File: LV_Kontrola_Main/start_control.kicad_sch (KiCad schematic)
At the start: 20 parts, among them U4 STM32F103C8Tx, Y1 32.768kHz, Y2 8MHz

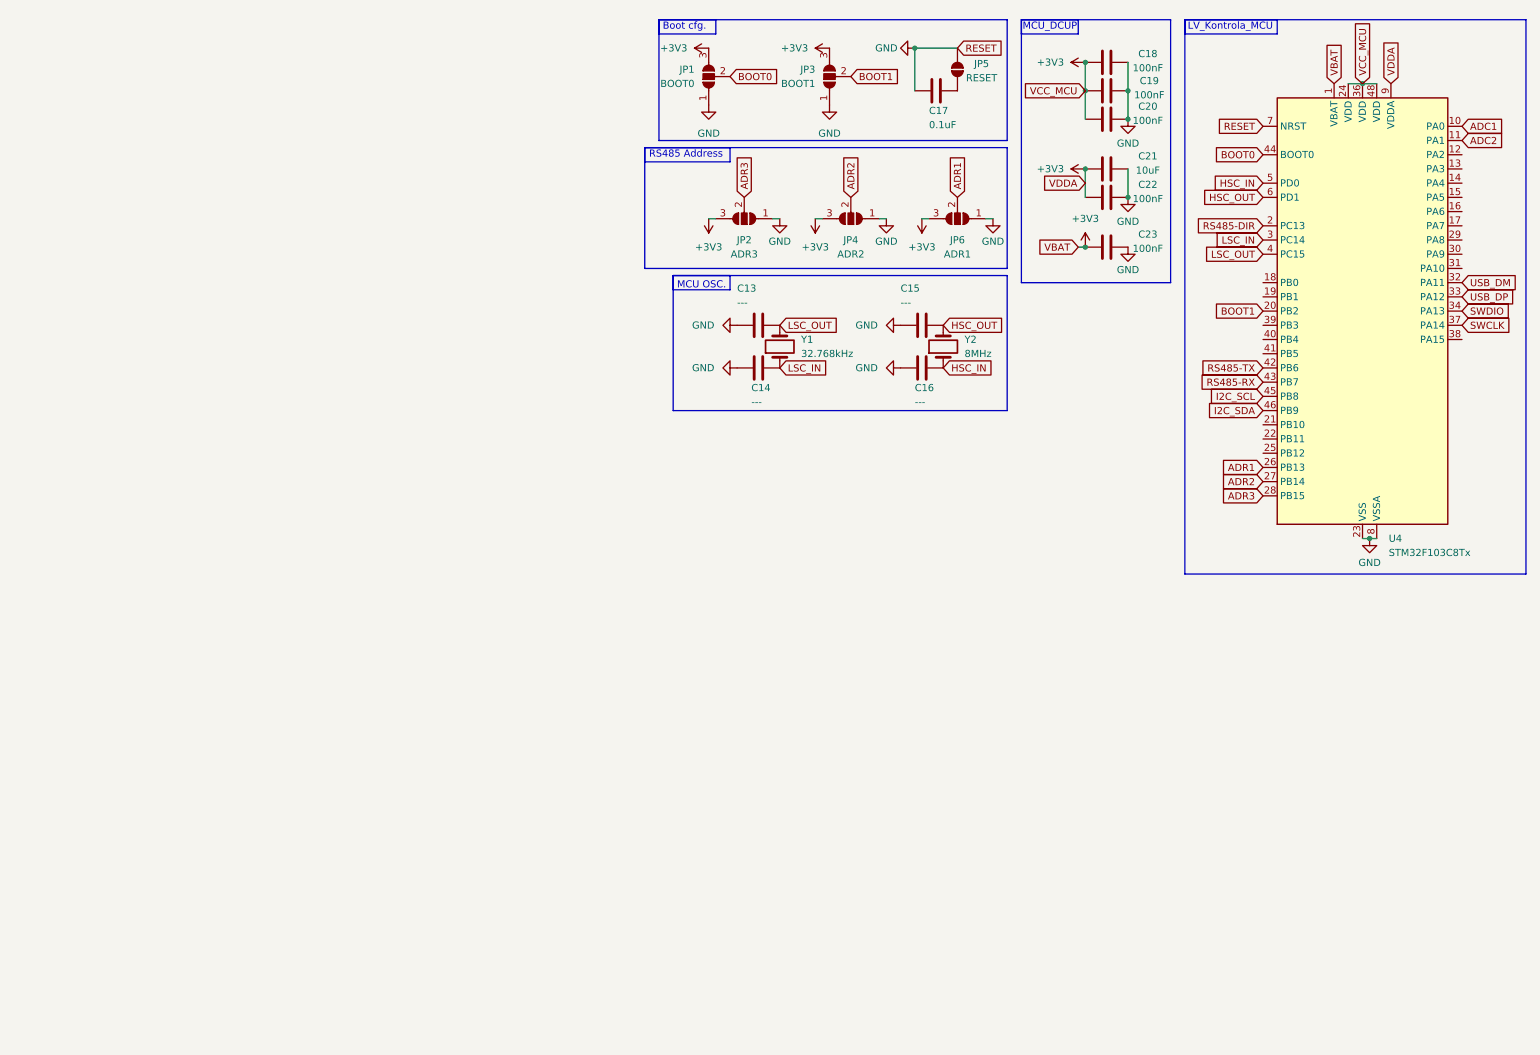
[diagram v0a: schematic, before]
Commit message: Added Start Control
Added Start Control MCU to the LV_Kontrola_Main, added hsc/lsc to LV_Regulator, fixed component numbering
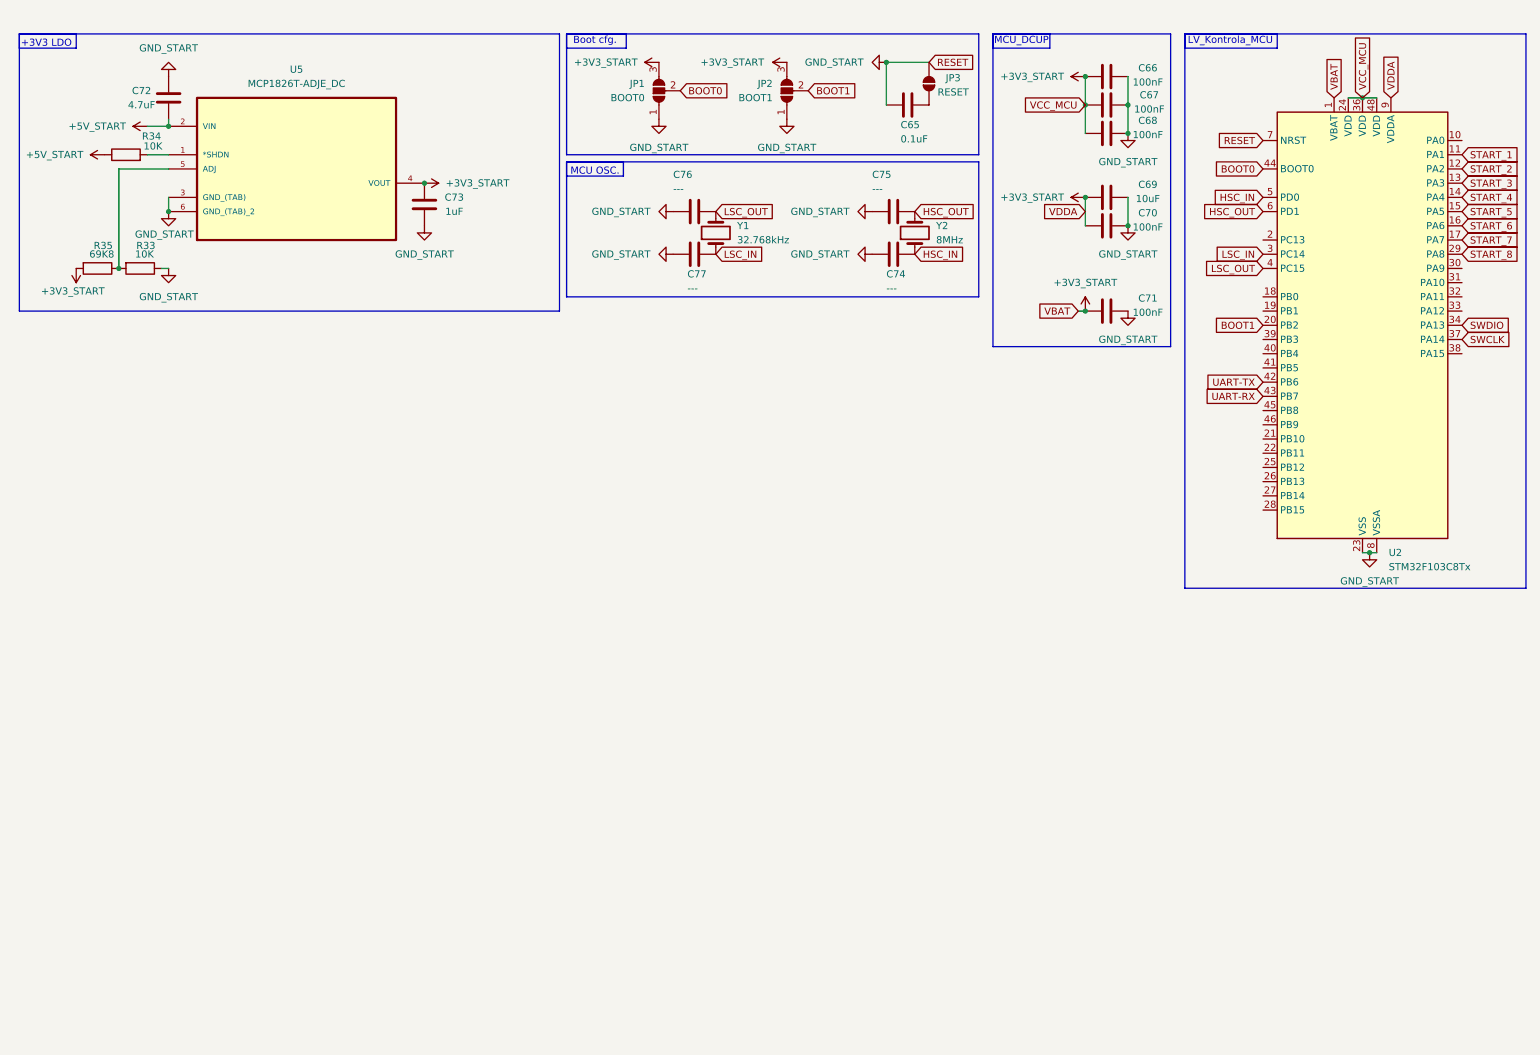
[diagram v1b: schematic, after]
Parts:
- removed C17: 0.1uF, symbol Device:C
- removed C18, C19, C20, C22, C23: 100nF, symbol Device:C
- removed C21: 10uF, symbol Device:C
- removed JP2: ADR3, symbol Jumper:SolderJumper_3_Open
- removed JP4: ADR2, symbol Jumper:SolderJumper_3_Open
- removed JP6: ADR1, symbol Jumper:SolderJumper_3_Open
- added C65: 0.1uF, symbol Device:C
- added C66, C67, C68, C70, C71: 100nF, symbol Device:C
- added C69: 10uF, symbol Device:C
- added C72: 4.7uF, symbol Device:C
- added C73: 1uF, symbol Device:C
- added R33, R34: 10K, symbol Device:R
- added R35: 69K8, symbol Device:R
- added U5: MCP1826T-ADJE_DC, MCP1826T-ADJE_DC:SOT230P700X180-6N, symbol MCP1826T-ADJE_DC:MCP1826T-ADJE_DC
- renumbered C16 to C74, C15 to C75, C13 to C76, C14 to C77, JP3 to JP2, JP5 to JP3, U4 to U2
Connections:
- net at JP3.2 (B): now also C65.1
- net START_2: now reaches U2.12 (PA2)
- net START_3: now reaches U2.13 (PA3)
- net START_4: now reaches U2.14 (PA4)
- net START_5: now reaches U2.15 (PA5)
- net START_6: now reaches U2.16 (PA6)
- net START_7: now reaches U2.17 (PA7)
- net START_8: now reaches U2.29 (PA8)
- net +3V3 renamed +3V3_START
- net +3V3_START: now also C66.1, C67.1, C68.1, C69.1, C70.1, C71.1, C73.2, R33.2, U5.4 (VOUT)
- net ADC1: no longer names the net of U2.10 (PA0)
- net ADC2 renamed START_1
- net ADR1: no longer names the net of U2.26 (PB13)
- net ADR2: no longer names the net of U2.27 (PB14)
- net ADR3: no longer names the net of U2.28 (PB15)
- net GND renamed GND_START
- net GND_START: now also C65.2, C66.2, C67.2, C68.2, C69.2, C70.2, C71.2, C72.1, C73.1, R35.1, U5.3 (GND_(TAB)), U5.6 (GND_(TAB)_2)
- net I2C_SCL: no longer names the net of U2.45 (PB8)
- net I2C_SDA: no longer names the net of U2.46 (PB9)
- net RS485-DIR: no longer names the net of U2.2 (PC13)
- net RS485-RX renamed UART-RX
- net RS485-TX renamed UART-TX
- net USB_DM: no longer names the net of U2.32 (PA11)
- net USB_DP: no longer names the net of U2.33 (PA12)
- new net: R34.2, U5.1 (*SHDN)
- new net: R33.1, R35.2, U5.5 (ADJ)
- new net +5V_START: C72.2, R34.1, U5.2 (VIN)
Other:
- note added: "+3V3 LDO"
- note removed: "RS485 Address"
- company: "Black Horntets" Formula Student team -> "Black Hornets" Formula Student team
- title: LV_Regulator_Main -> LV_Kontrola_Main
- moved on the sheet: C74, C75, C76, C77, JP1, JP2, JP3, U2, Y1, Y2

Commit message: Added Stat logic
Added start mcu and associated components to the LV_Kontrola_Main schematic, added STM32CubeIDE project and basic configuration, added fuses to LV_Regulator
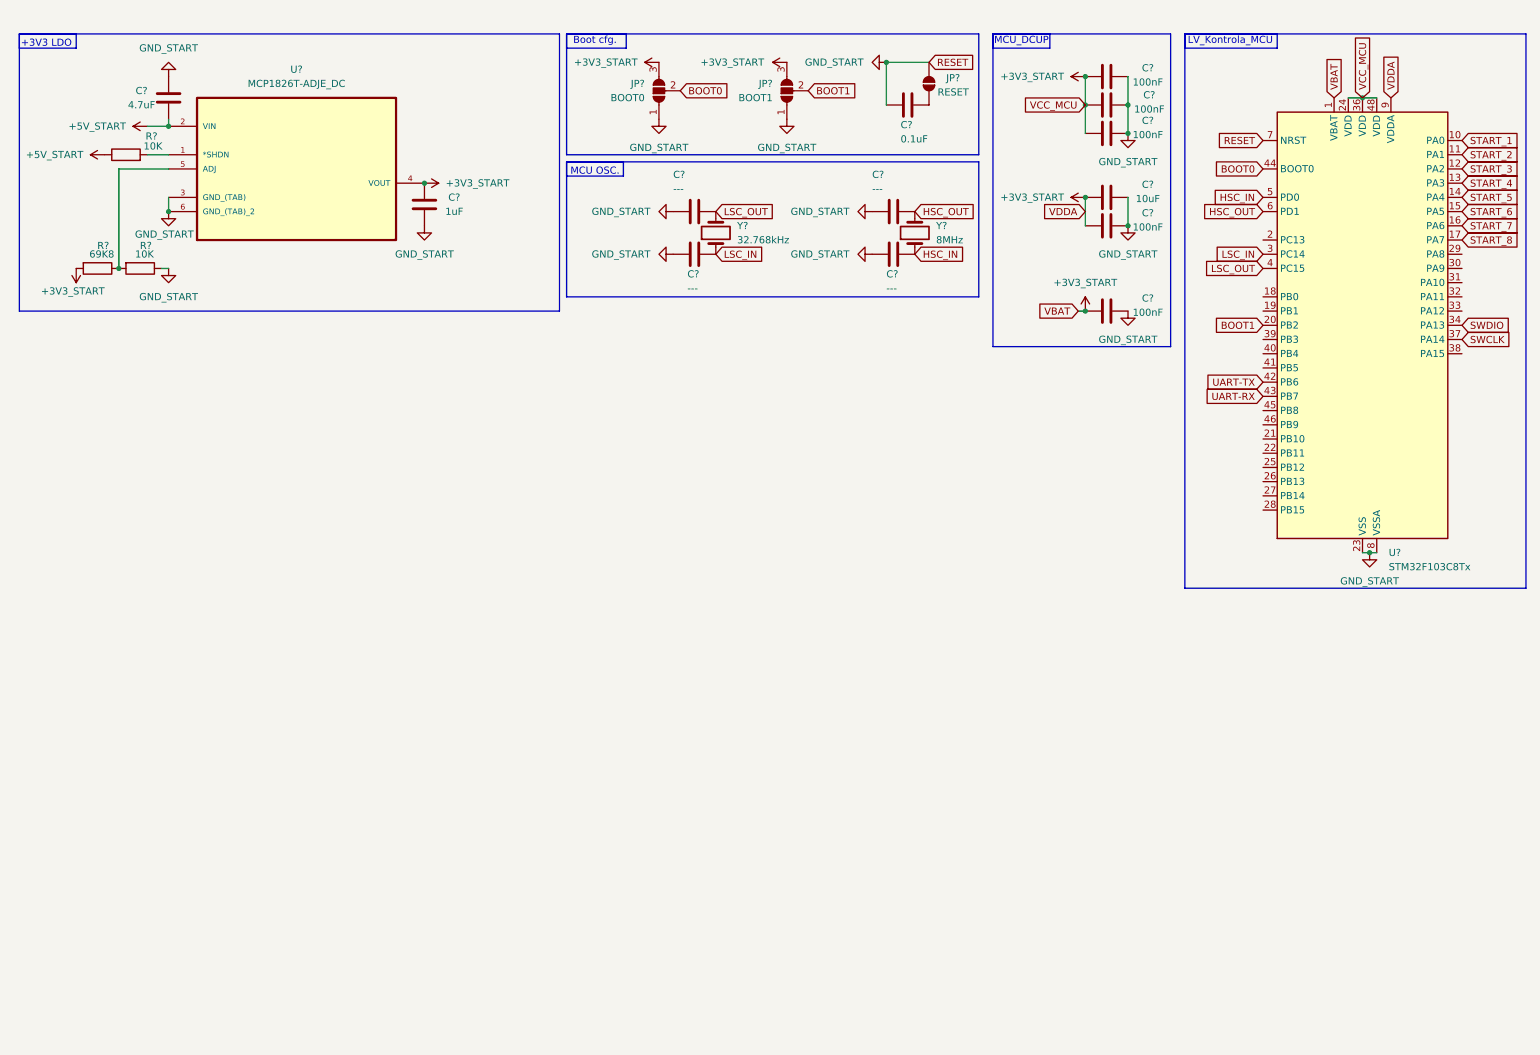
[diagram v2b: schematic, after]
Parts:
- renumbered C76 to C?, C68 to C?, C72 to C?, C74 to C?, C71 to C?, C67 to C?, C70 to C?, C66 to C?, C77 to C?, C65 to C?, C75 to C?, C73 to C?, C69 to C?, JP2 to JP?, JP1 to JP?, JP3 to JP?, R34 to R?, R35 to R?, R33 to R?, U5 to U?, U2 to U?, Y1 to Y?, Y2 to Y?
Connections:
- net START_1: now also U?.10 (PA0); no longer U?.11 (PA1)
- net START_2: now also U?.11 (PA1); no longer U?.12 (PA2)
- net START_3: now also U?.12 (PA2); no longer U?.13 (PA3)
- net START_4: now also U?.13 (PA3); no longer U?.14 (PA4)
- net START_5: now also U?.14 (PA4); no longer U?.15 (PA5)
- net START_6: now also U?.15 (PA5); no longer U?.16 (PA6)
- net START_7: now also U?.16 (PA6); no longer U?.17 (PA7)
- net START_8: now also U?.17 (PA7); no longer U?.29 (PA8)

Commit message: Various changes
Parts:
- removed C?: 4.7uF, symbol Device:C
- removed C?: 1uF, symbol Device:C
- removed R? (x2): 10K, symbol Device:R
- removed R?: 69K8, symbol Device:R
- removed U?: MCP1826T-ADJE_DC, MCP1826T-ADJE_DC:SOT230P700X180-6N, symbol MCP1826T-ADJE_DC:MCP1826T-ADJE_DC
- added C78, C79, C80: 100nF, symbol Device:C
- added J5: SWD, symbol Connector:Conn_01x04_Pin
- added J6: 2169890001, USB-C:MOLEX_2169890001, symbol 2169890001:2169890001
- added JP4: ADR2, symbol Jumper:SolderJumper_3_Open
- added JP6: ADR1, symbol Jumper:SolderJumper_3_Open
- added R118, R119: 27R, Resistor_SMD:R_1206_3216Metric_Pad1.30x1.75mm_HandSolder, symbol Device:R
- added R120: 1K5, Resistor_SMD:R_1206_3216Metric_Pad1.30x1.75mm_HandSolder, symbol Device:R
- added R121, R122: 5K1, Resistor_SMD:R_1206_3216Metric_Pad1.30x1.75mm_HandSolder, symbol Device:R
- added R36, R37: ---, symbol Device:R
- added R38: 120, symbol Device:R
- added U1: ADM2483xRW, Package_SO:SOIC-16W_7.5x10.3mm_P1.27mm, symbol Interface_UART:ADM2483xRW
- gave numbers to parts that had none: 17
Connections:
- net +3V3_START: now also C78.2, C80.1, J5.1 (Pin_1), JP4.3 (B), JP6.3 (B), R120.1, U1.1 (VDD1), U1.7 (PV)
- net +5V_START: now also C79.2, R37.2, U1.16 (VDD2)
- net GND_START: now also C78.1, C79.1, C80.2, J5.4 (Pin_4), J6.A1 (GND1), J6.A12 (GND2), J6.B1 (GND3), J6.B12 (GND4), J6.SH1 (SHIELD1), J6.SH2 (SHIELD2), J6.SH3 (SHIELD3), J6.SH4 (SHIELD4), JP4.1 (A), JP6.1 (A), R121.1, R122.2, R36.1, U1.15 (GND2), U1.2 (GND1), U1.8 (GND1), U1.9 (GND2)
- net SWCLK: now also J5.3 (Pin_3)
- net SWDIO: now also J5.2 (Pin_2)
- net RS485-DIR: now reaches U2.2 (PC13)
- net RS485-DIR: now also U1.4 (~{RE}), U1.5 (DE)
- net USB_DM: now reaches U2.32 (PA11)
- net USB_DM: now also R118.2
- net USB_DP: now reaches U2.33 (PA12)
- net USB_DP: now also R119.1
- net UART-RX renamed RS485-RX
- net RS485-RX: now also U1.3 (RxD)
- net UART-TX renamed RS485-TX
- net RS485-TX: now also U1.6 (TxD)
- new net: J6.A5 (CC1), R122.1
- new net: J6.B5 (CC2), R121.2
- new net ADR1: JP6.2 (C)
- new net ADR2: JP4.2 (C)
- new net CON_DN: J6.A7 (DA-), J6.B7 (DB-), R118.1
- new net CON_DP: J6.A6 (DA+), J6.B6 (DB+), R119.2, R120.2
- new net RS485-A: R37.1, R38.2, U1.12 (A)
- new net RS485-B: R36.2, R38.1, U1.13 (B)
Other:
- note added: "NO ISOLATION !!!"
- note added: "RS485 Address"
- note added: "RS485 Transiver"
- note added: "SWD"
- note added: "USB"
- note removed: "+3V3 LDO"
- moved on the sheet: C65, C66, C67, C68, C69, C70, C71, C74, C75, C76, C77, JP1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

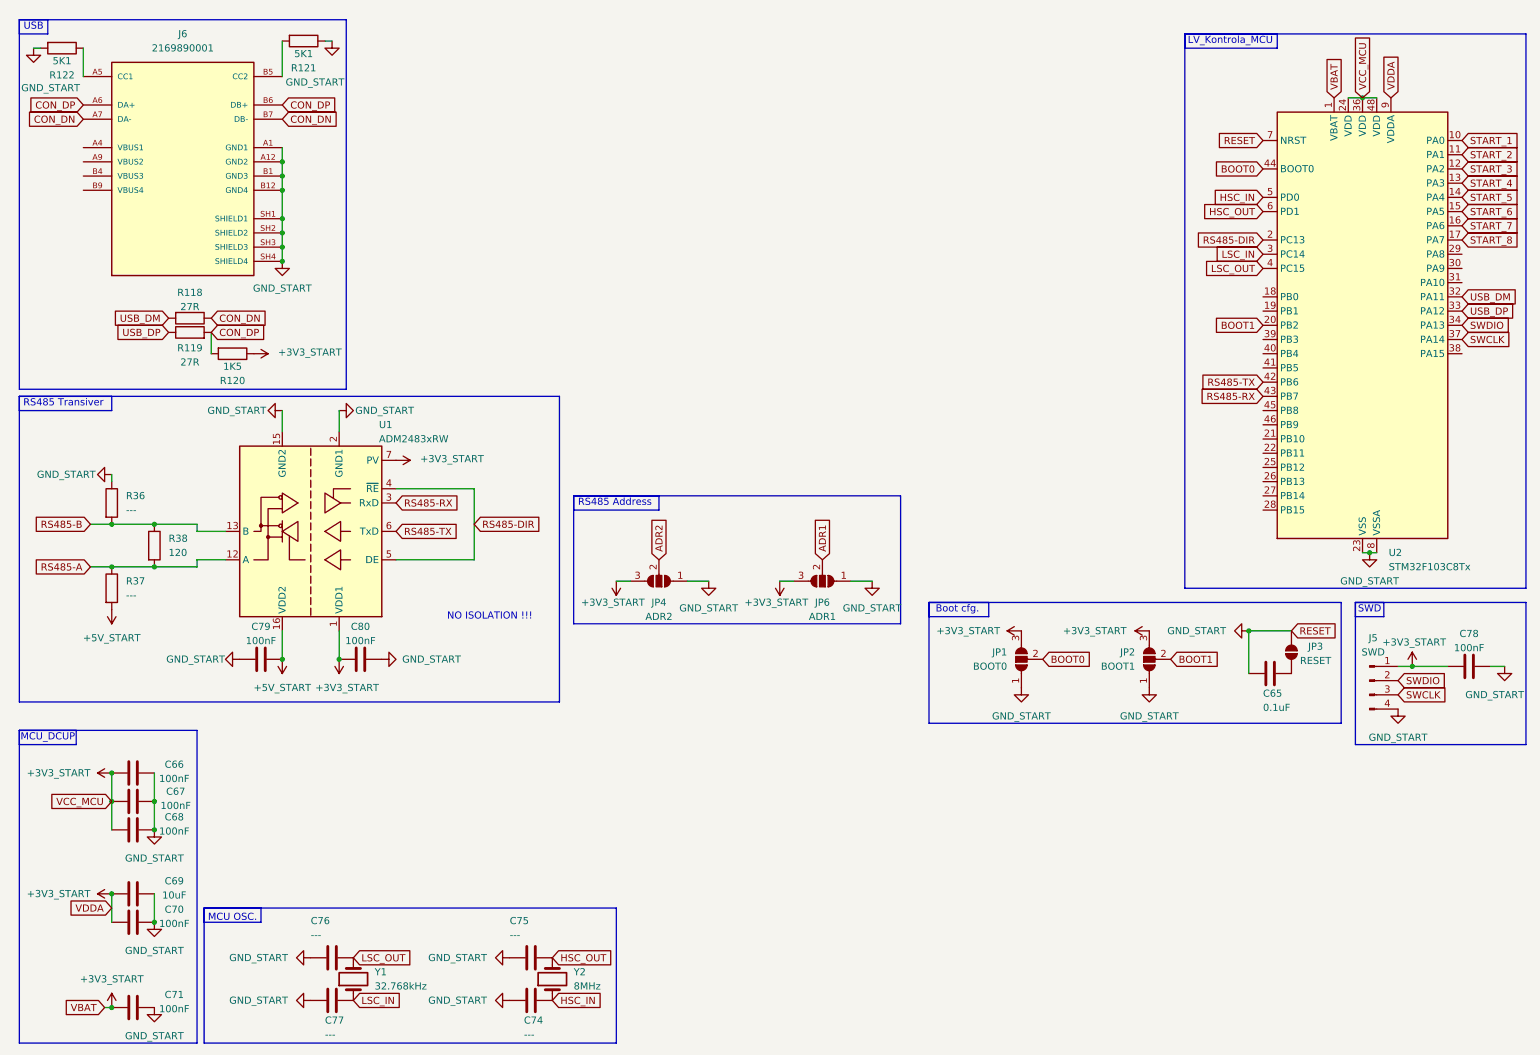
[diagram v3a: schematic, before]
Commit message: Changes to LV_Kontrola_Main
Added a lot to the schematic, fixed component libs, mics...
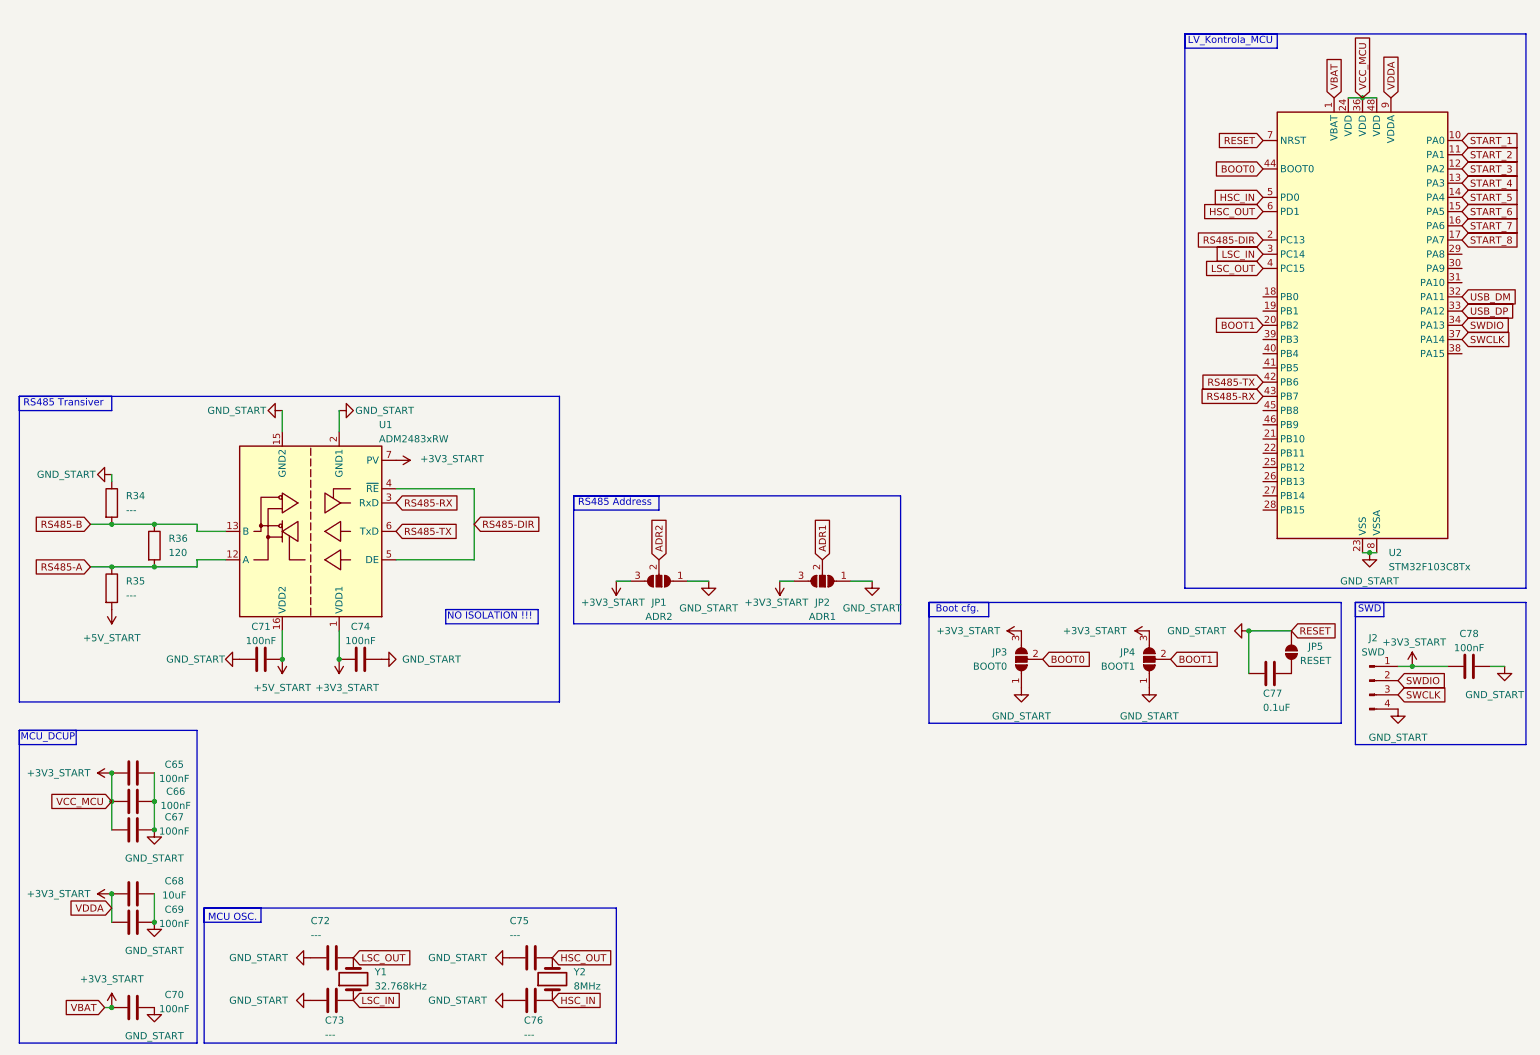
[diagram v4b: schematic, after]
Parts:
- removed J6: 2169890001, USB-C:MOLEX_2169890001, symbol 2169890001:2169890001
- removed R118, R119: 27R, Resistor_SMD:R_1206_3216Metric_Pad1.30x1.75mm_HandSolder, symbol Device:R
- removed R120: 1K5, Resistor_SMD:R_1206_3216Metric_Pad1.30x1.75mm_HandSolder, symbol Device:R
- removed R121, R122: 5K1, Resistor_SMD:R_1206_3216Metric_Pad1.30x1.75mm_HandSolder, symbol Device:R
- renumbered C66 to C65, C67 to C66, C68 to C67, C69 to C68, C70 to C69, C71 to C70, C79 to C71, C76 to C72, C77 to C73, C80 to C74, C74 to C76, C65 to C77, J5 to J2, JP4 to JP1, JP6 to JP2, JP1 to JP3, JP2 to JP4, JP3 to JP5, R36 to R34, R37 to R35, R38 to R36
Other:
- note removed: "USB"
